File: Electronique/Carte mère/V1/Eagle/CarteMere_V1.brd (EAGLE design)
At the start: 95 x 80.1 mm, 25 parts, among them J100 BP_Rouge, J101 BP Jaune, J102 BP Vert, J600 LED_VERTE, J601 LED_JAUNE, J602 LED_ROUGE, Q500 SI2303DS, Q501 SI2302DS, U200 FIREBEETLE-ESP32-DFR0478, U300 RTC_ADA-3295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

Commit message: ajout trou pour maintien Carte SD
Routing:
- net 3V3: track 135.9 -> 134.8 mm
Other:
- outline, holes or cut-outs redrawn

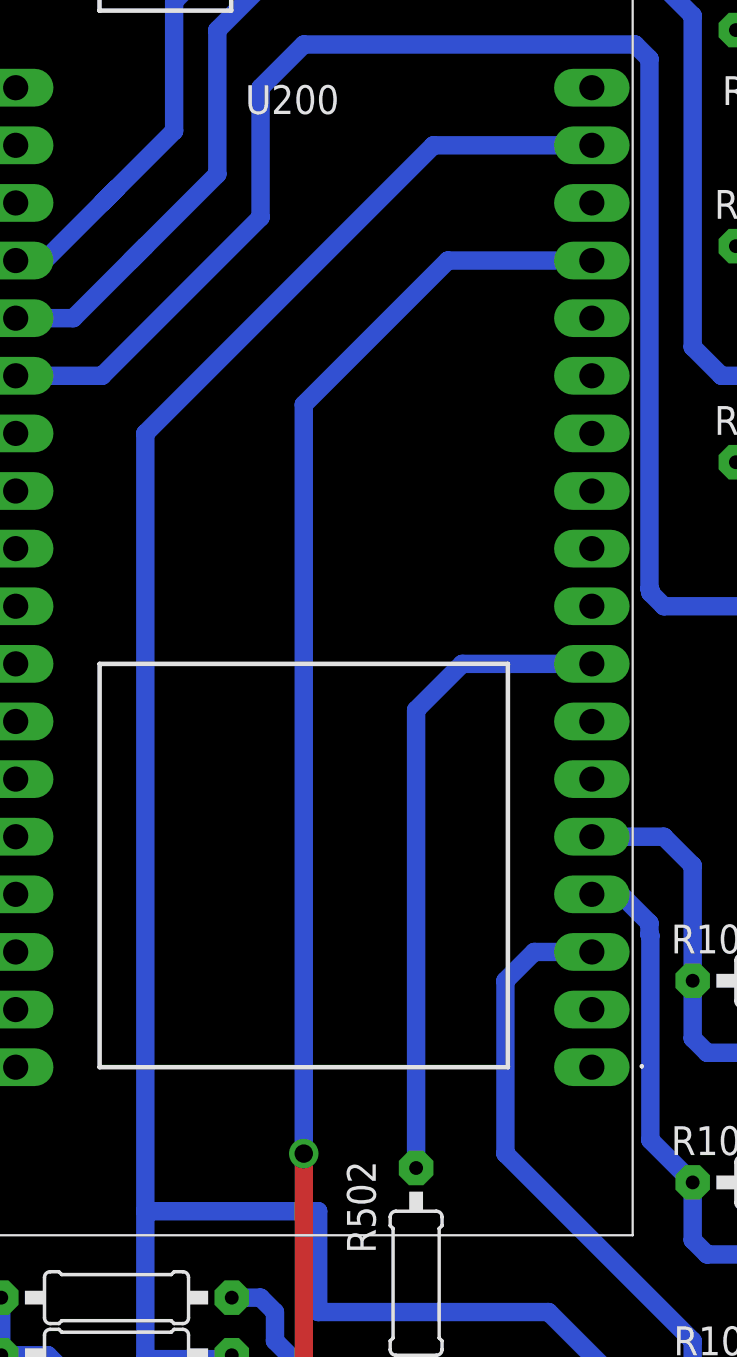
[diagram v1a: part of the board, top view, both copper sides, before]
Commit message: Modif dimension ligne alim
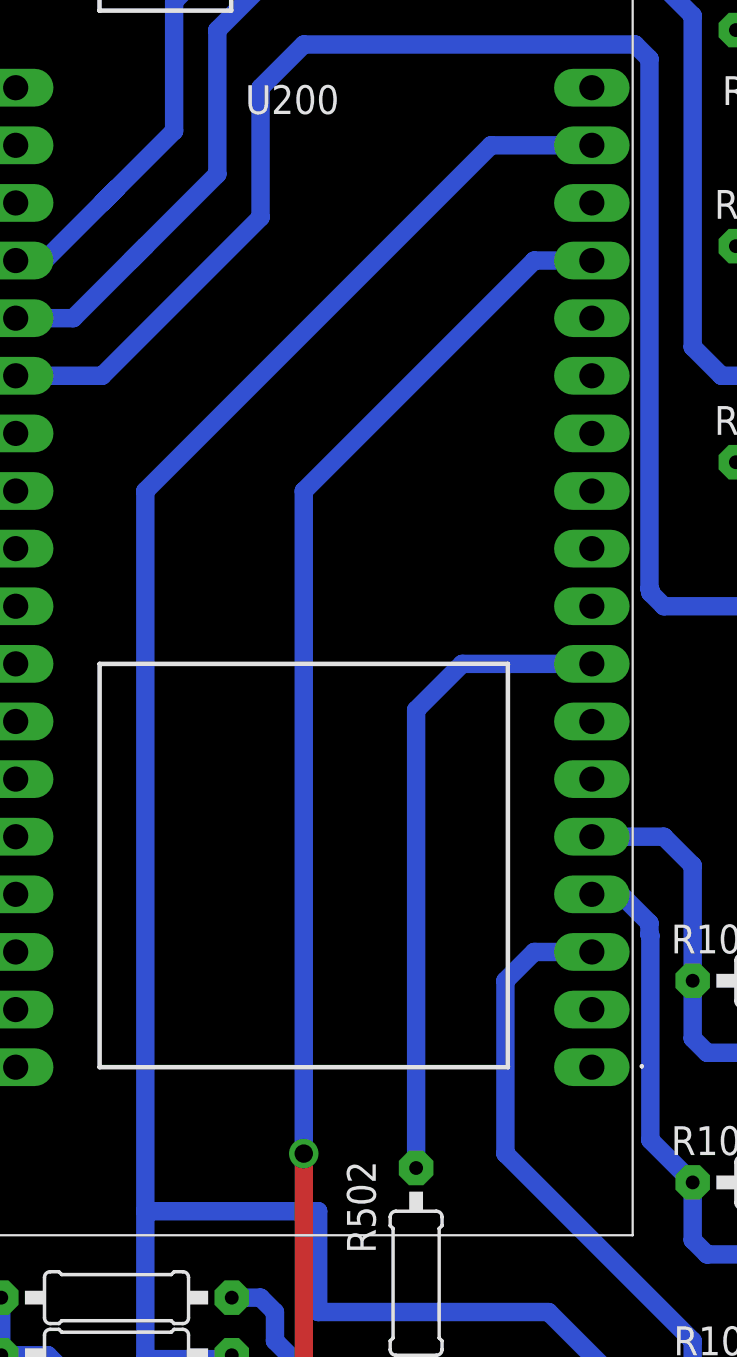
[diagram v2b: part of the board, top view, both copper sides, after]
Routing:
- net GND: track 291.6 -> 289.4 mm
- net 3V3: track 134.8 -> 133.3 mm
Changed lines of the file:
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@@
 <setting verticaltext="up"/>
 </settings>
-<grid distance="0.5" unitdist="mm" unit="mm" style="lines" multiple="1" display="no" altdistance="0.05" altunitdist="mm" altunit="mm"/>
+<grid distance="50" unitdist="mil" unit="mil" style="lines" multiple="1" display="no" altdistance="5" altunitdist="mm" altunit="mm"/>
 <layers>
 <layer number="1" name="Top" color="4" fill="1" visible="yes" active="yes"/>
@@
 <wire x1="55.88" y1="6.985" x2="55.88" y2="1.81" width="0.8128" layer="16"/>
 <wire x1="71.12" y1="1.81" x2="55.88" y2="1.81" width="0.8128" layer="16"/>
-<wire x1="55.88" y1="57.15" x2="62.23" y2="63.5" width="0.8128" layer="16"/>
-<wire x1="62.23" y1="63.5" x2="68.58" y2="63.5" width="0.8128" layer="16"/>
-<wire x1="55.88" y1="57.15" x2="55.88" y2="24.13" width="0.8128" layer="16"/>
+<wire x1="68.58" y1="63.5" x2="66.04" y2="63.5" width="0.8128" layer="16"/>
+<wire x1="55.88" y1="53.34" x2="55.88" y2="24.13" width="0.8128" layer="16"/>
 <wire x1="55.88" y1="6.985" x2="55.88" y2="24.13" width="0.8128" layer="1"/>
 <wire x1="71.12" y1="1.81" x2="71.12" y2="6.985" width="0.8128" layer="16"/>
@@
 <wire x1="81.28" y1="1.81" x2="83.185" y2="3.715" width="0.8128" layer="16"/>
 <wire x1="83.185" y1="3.715" x2="83.185" y2="13.97" width="0.8128" layer="16"/>
+<wire x1="66.04" y1="63.5" x2="55.88" y2="53.34" width="0.8128" layer="16"/>
 </signal>
 <signal name="I2C_SDA">
@@
 <wire x1="56.515" y1="21.59" x2="56.515" y2="17.145" width="0.8128" layer="16"/>
 <wire x1="56.515" y1="21.59" x2="48.895" y2="21.59" width="0.8128" layer="16"/>
-<wire x1="48.895" y1="21.59" x2="48.895" y2="55.88" width="0.8128" layer="16"/>
+<wire x1="48.895" y1="21.59" x2="48.895" y2="53.34" width="0.8128" layer="16"/>
 <wire x1="56.515" y1="17.145" x2="66.675" y2="17.145" width="0.8128" layer="16"/>
 <wire x1="52.705" y1="15.24" x2="52.535" y2="15.07" width="0.8128" layer="16"/>
@@
 <wire x1="78.105" y1="15.24" x2="78.105" y2="17.145" width="0.8128" layer="16"/>
 <wire x1="80.01" y1="8.255" x2="81.28" y2="9.525" width="0.8128" layer="16"/>
-<wire x1="48.895" y1="55.88" x2="61.595" y2="68.58" width="0.8128" layer="16"/>
-<wire x1="61.595" y1="68.58" x2="68.58" y2="68.58" width="0.8128" layer="16"/>
+<wire x1="48.895" y1="53.34" x2="64.135" y2="68.58" width="0.8128" layer="16"/>
+<wire x1="64.135" y1="68.58" x2="68.58" y2="68.58" width="0.8128" layer="16"/>
 </signal>
 <signal name="BP_VERT">
